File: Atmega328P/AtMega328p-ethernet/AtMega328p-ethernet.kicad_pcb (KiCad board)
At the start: 4 copper layers, 66.5 x 50 mm, 77 parts, among them J1 Conn_01x06_Socket, J2 USB_C_Receptacle_USB2.0_12P, J4 Conn_01x06_Socket, J5 Conn_01x06_Socket, J6 Conn_01x06_Socket, J7 Conn_01x06_Socket, J8 Conn_02x03_Counter_Clockwise, J9 RJ45_Hanrun_HR911105A_Horizon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, SW1 SW_Push, U1 ATmega328P-A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

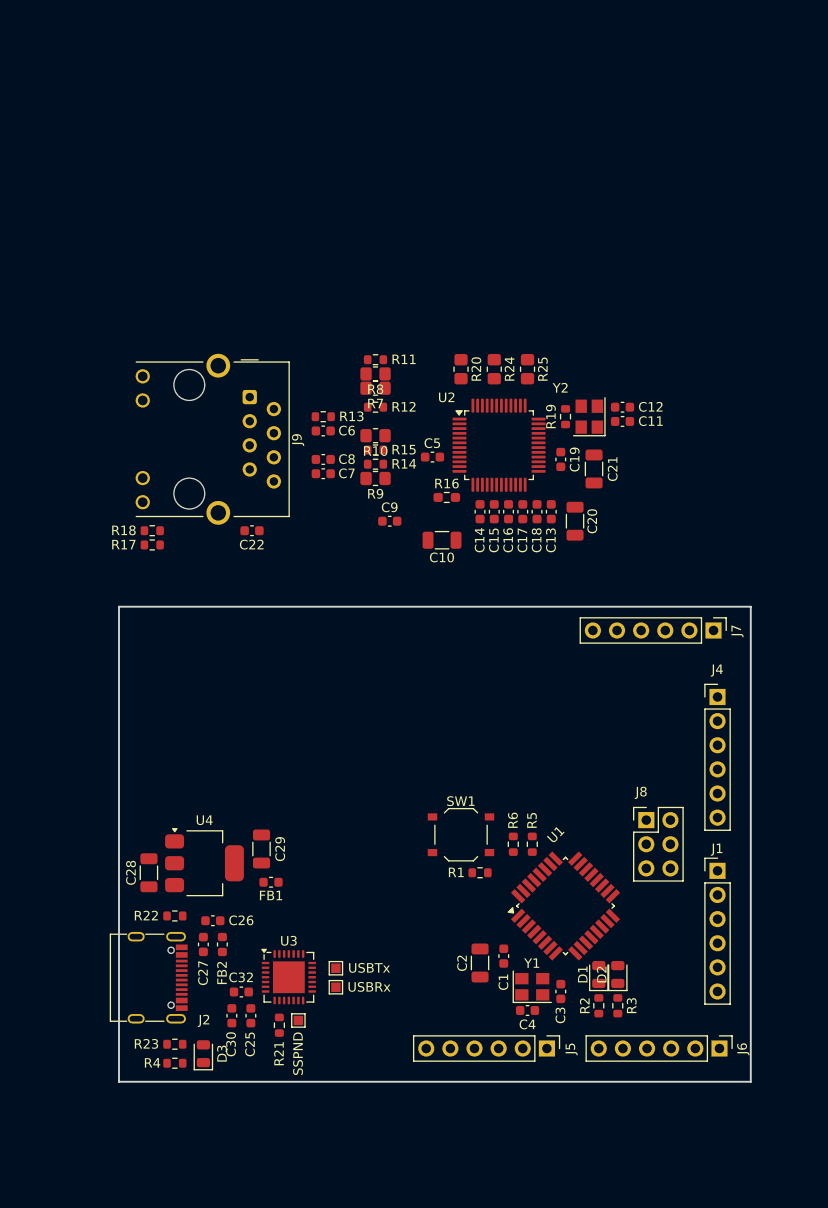
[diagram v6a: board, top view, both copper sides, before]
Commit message: Most components layed out and locked still to do ethernet
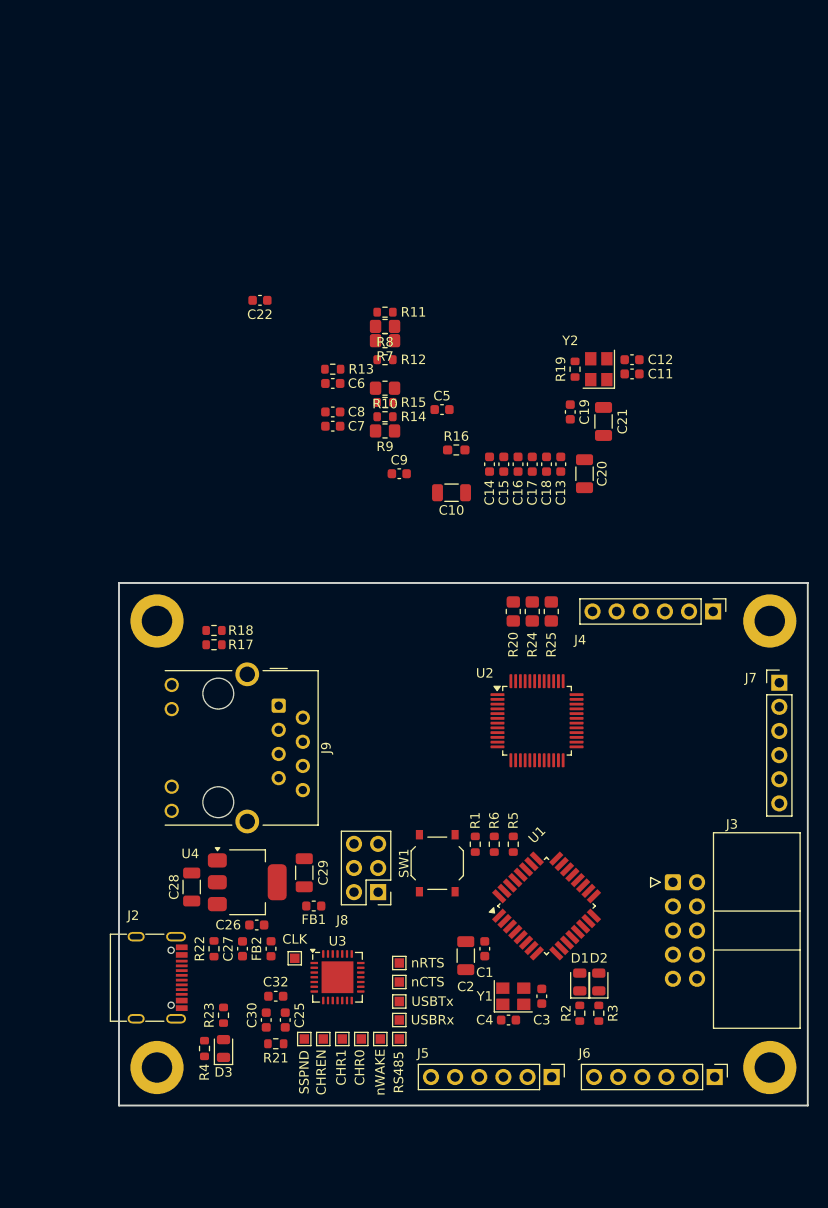
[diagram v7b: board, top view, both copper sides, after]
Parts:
- removed J1: Conn_01x06_Socket, Connector_PinHeader_2.54mm:PinHeader_1x06_P2.54mm_Vertical
- added H1: MountingHole_Pad, MountingHole:MountingHole_3.2mm_M3_DIN965_Pad, F.Cu at (104.0, 101.5)
- added H2: MountingHole_Pad, MountingHole:MountingHole_3.2mm_M3_DIN965_Pad, F.Cu at (168.5, 101.5)
- added H3: MountingHole_Pad, MountingHole:MountingHole_3.2mm_M3_DIN965_Pad, F.Cu at (168.5, 148.5)
- added H4: MountingHole_Pad, MountingHole:MountingHole_3.2mm_M3_DIN965_Pad, F.Cu at (104.0, 148.5)
- added J3: Conn_02x05_Odd_Even, Connector_IDC:IDC-Header_2x05_P2.54mm_Horizontal, F.Cu at (158.3, 129.0)
- added TP10: CHR1, TestPoint:TestPoint_Pad_1.0x1.0mm, F.Cu at (123.5, 145.5)
- added TP11: RS485, TestPoint:TestPoint_Pad_1.0x1.0mm, F.Cu at (129.5, 145.5)
- added TP12: nWAKE, TestPoint:TestPoint_Pad_1.0x1.0mm, F.Cu at (127.5, 145.5)
- added TP5: nRTS, TestPoint:TestPoint_Pad_1.0x1.0mm, F.Cu at (129.5, 137.5)
- added TP6: nCTS, TestPoint:TestPoint_Pad_1.0x1.0mm, F.Cu at (129.5, 139.5)
- added TP7: CLK, TestPoint:TestPoint_Pad_1.0x1.0mm, F.Cu at (118.5, 137.0)
- added TP8: CHREN, TestPoint:TestPoint_Pad_1.0x1.0mm, F.Cu at (121.5, 145.5)
- added TP9: CHR0, TestPoint:TestPoint_Pad_1.0x1.0mm, F.Cu at (125.5, 145.5)
- moved J9 32.6 mm to (116.8, 110.4)
- moved U2 29.3 mm to (144.0, 112.0)
- moved J8 29.2 mm to (127.3, 130.0), turned to 180 degrees
- moved R20 26.1 mm to (141.5, 100.5)
- moved R24 25.8 mm to (143.5, 100.5)
- moved R25 25.6 mm to (145.5, 100.5)
- moved C22 24.3 mm to (114.8, 67.8)
- moved R17 12.3 mm to (110.0, 104.0)
- moved R18 12.3 mm to (110.0, 102.5)
- moved J4 9.01 mm to (162.5, 100.5), turned to -90 degrees
- moved J7 8.84 mm to (169.5, 108.0), turned to 0 degrees
- moved TP4 7.53 mm to (129.5, 141.6)
- moved TP3 7.51 mm to (129.5, 143.5)
- moved R23 5.96 mm to (111.0, 143.0), turned to 90 degrees
- moved R22 5.37 mm to (110.0, 136.0), turned to -90 degrees
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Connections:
- U1 pad 14: GND -> /ETH_SPI_SS
- U2 pad 35: GND -> /ETH_SPI_SS
- U3 pad 13: unconnected-(U3-CHREN-Pad13) -> Net-(U3-CHREN)
- U3 pad 14: unconnected-(U3-CHR1-Pad14) -> Net-(U3-CHR1)
- U3 pad 15: unconnected-(U3-CHR0-Pad15) -> Net-(U3-CHR0)
- U3 pad 16: unconnected-(U3-~{WAKEUP}/GPIO.3-Pad16) -> Net-(U3-~{WAKEUP}/GPIO.3)
- U3 pad 17: unconnected-(U3-RS485/GPIO.2-Pad17) -> Net-(U3-RS485/GPIO.2)
- U3 pad 2: unconnected-(U3-~{RI}/CLK-Pad2) -> Net-(U3-~{RI}/CLK)
- U3 pad 23: unconnected-(U3-~{CTS}-Pad23) -> Net-(U3-~{CTS})
- U3 pad 24: unconnected-(U3-~{RTS}-Pad24) -> Net-(U3-~{RTS})
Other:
- board size 66.5 x 50 mm -> 72.5 x 55 mm

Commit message: Layout complete ready for review
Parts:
- added J10: Conn_02x03_Counter_Clockwise, Connector_PinHeader_2.54mm:PinHeader_2x03_P2.54mm_Vertical, F.Cu at (155.0, 109.5)
- C10: footprint Capacitor_SMD:C_1206_3216Metric -> Capacitor_SMD:C_0805_2012Metric
- R16: footprint Resistor_SMD:R_0603_1608Metric_Pad0.98x0.95mm_HandSolder -> Resistor_SMD:R_0805_2012Metric_Pad1.20x1.40mm_HandSolder
- moved C22 53.8 mm to (125.5, 120.5)
- moved R11 42.0 mm to (128.0, 111.0), turned to -90 degrees
- moved R8 40.2 mm to (132.0, 110.5)
- moved C5 39.7 mm to (125.5, 118.0)
- moved C20 39.1 mm to (132.5, 121.5)
- moved C9 39.1 mm to (148.0, 120.5), turned to -90 degrees
- moved C11 38.7 mm to (158.0, 114.0)
- moved C12 38.7 mm to (158.0, 112.5)
- moved R19 38.7 mm to (152.0, 113.5)
- moved Y2 38.7 mm to (154.5, 113.5)
- moved R10 38.2 mm to (132.0, 115.0)
- moved C19 37.7 mm to (151.0, 117.0)
- moved C21 37.6 mm to (153.0, 118.0)
- moved R14 37.5 mm to (128.0, 117.5), turned to 90 degrees
- moved C6 37.1 mm to (125.5, 113.5)
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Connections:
- net /ETHERNET_MODULE/ETH_RXN renamed /ETHERNET_MODULE/ETH_RX_N
- net /ETHERNET_MODULE/ETH_RXN_C renamed /ETHERNET_MODULE/ETH_C_RX_N
- net /ETHERNET_MODULE/ETH_RXP renamed /ETHERNET_MODULE/ETH_RX_P
- net /ETHERNET_MODULE/ETH_RXP_C renamed /ETHERNET_MODULE/ETH_C_RX_P
- net /ETHERNET_MODULE/ETH_TXN renamed /ETHERNET_MODULE/ETH_TX_N
- net /ETHERNET_MODULE/ETH_TXN_C renamed /ETHERNET_MODULE/ETH_C_TX_N
- net /ETHERNET_MODULE/ETH_TXP renamed /ETHERNET_MODULE/ETH_TX_P
- net /ETHERNET_MODULE/ETH_TXP_C renamed /ETHERNET_MODULE/ETH_C_TX_P
- J3 pad 10: /GPIO3 -> /PC0
- J3 pad 8: /GPIO2 -> /PD5
- J3 pad 9: /GPIO1 -> /PB2
- J4 pad 1: +5V -> +3.3V
- J7 pad 1: +5V -> +3.3V
- J8 pad 2: /SPI_SCK -> +5V
- J8 pad 3: /nRST -> /SPI_SCK
- J8 pad 4: GND -> /SPI_MOSI
- J8 pad 5: /SPI_MOSI -> /nRST
- J8 pad 6: +5V -> GND
- U1 pad 14: /ETH_SPI_SS -> /PB2
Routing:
- added copper zone on In2.Cu, net +3.3V
- added copper zone on In2.Cu, net /ETHERNET_MODULE/+3.3VA_IN
